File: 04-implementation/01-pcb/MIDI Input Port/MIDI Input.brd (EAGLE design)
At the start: 102.9 x 29.8 mm, 38 parts, among them J1 SDS-50J, J2 SDS-50J, J3 SDS-50J, J4 SDS-50J, J5 SSW-107-02-S-D, U1 PC900V, U2 PC900V, U3 PC900V, U4 PC900V

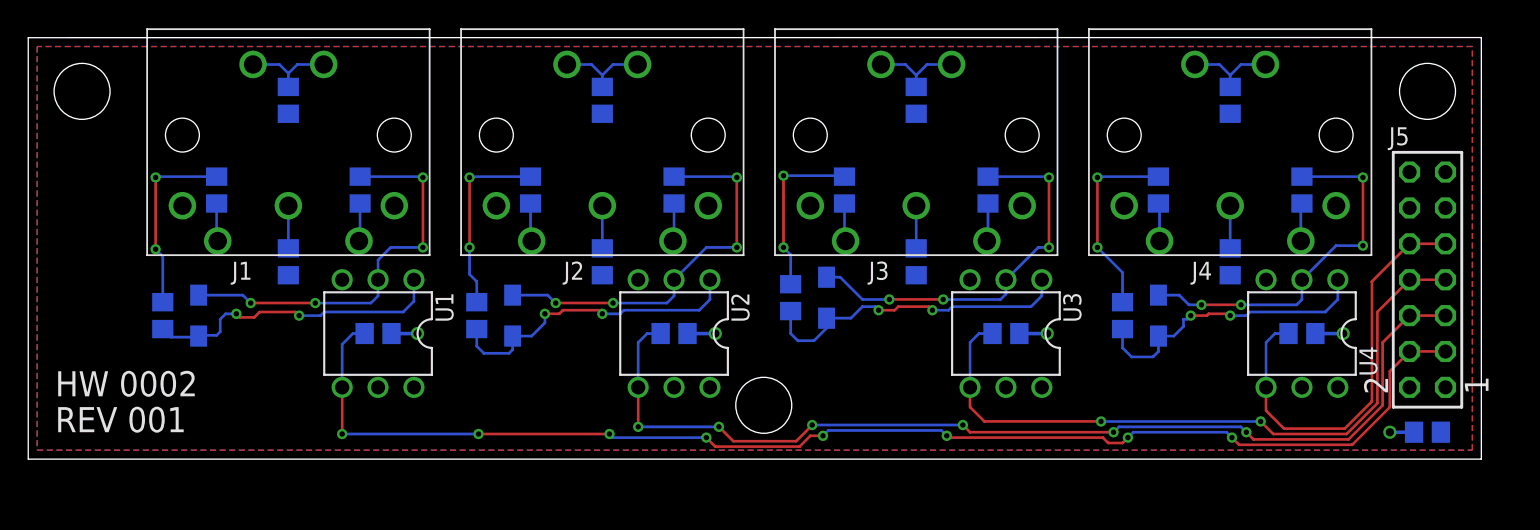
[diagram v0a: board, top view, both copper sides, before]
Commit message: Revise MIDI PCB's for mechanical spacing of ribbon connector.
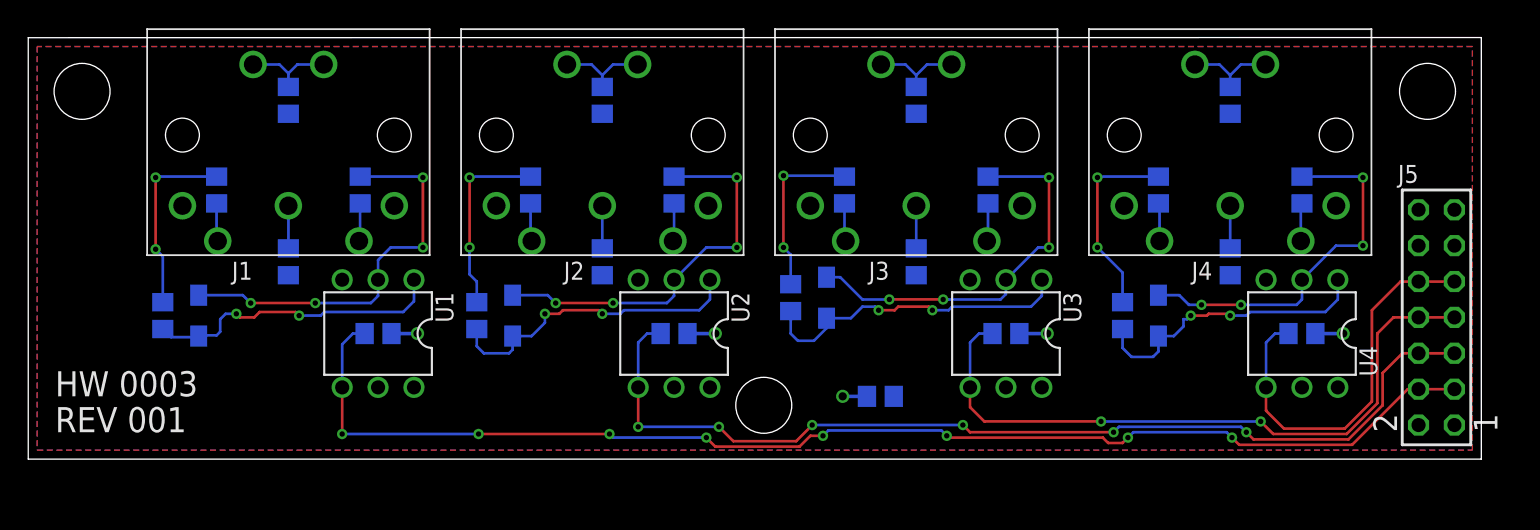
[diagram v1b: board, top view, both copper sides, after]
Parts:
- moved C9 38.8 mm to (60.3, 4.45)
- moved J5 2.74 mm to (99.7, 10.0)
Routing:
- net D-IN1: track 92.5 -> 90.5 mm
- net D-IN2: track 72.8 -> 71.1 mm
- net D-IN4: track 30.3 -> 28.6 mm
- net D-IN3: track 49.2 -> 47.8 mm
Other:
- board text added: "HW 0003"
- board text removed: "HW 0002"
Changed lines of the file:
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@@
 <?xml version="1.0" encoding="utf-8"?>
 <!DOCTYPE eagle SYSTEM "eagle.dtd">
-<eagle version="8.4.0">
+<eagle version="9.0.1">
 <drawing>
 <settings>
@@
 <setting verticaltext="up"/>
 </settings>
-<grid distance="25" unitdist="mil" unit="mil" style="lines" multiple="1" display="yes" altdistance="5" altunitdist="mil" altunit="mil"/>
+<grid distance="5" unitdist="mil" unit="mil" style="lines" multiple="1" display="yes" altdistance="5" altunitdist="mil" altunit="mil"/>
 <layers>
 <layer number="1" name="Top" color="4" fill="1" visible="yes" active="yes"/>
@@
 <hole x="52.07" y="3.81" drill="3.9624"/>
 <hole x="99.06" y="26.035" drill="3.9624"/>
-<text x="1.905" y="4.445" size="1.778" layer="25">HW 0002</text>
+<text x="1.905" y="4.445" size="1.778" layer="25">HW 0003</text>
 <text x="1.905" y="1.905" size="1.778" layer="25">REV 001</text>
 </plain>
@@
 <param name="dpMaxLengthDifference" value="10mm"/>
 <param name="dpGapFactor" value="2.5"/>
+<param name="checkAngle" value="0"/>
 <param name="checkFont" value="1"/>
 <param name="checkRestrict" value="1"/>
 <param name="checkStop" value="0"/>
+<param name="checkValues" value="0"/>
 <param name="useDiameter" value="13"/>
 <param name="maxErrors" value="50"/>
@@
 <attribute name="VALUE" x="20.955" y="15.24" size="1.27" layer="28" rot="MR270"/>
 </element>
-<element name="J5" library="con-samtec" library_urn="urn:adsk.eagle:library:184" package="SSW-107-02-S-D" value="SSW-107-02-S-D" x="99.06" y="12.7" smashed="yes" rot="R90">
-<attribute name="MF" value="" x="99.06" y="12.7" size="1.778" layer="27" rot="R90" display="off"/>
-<attribute name="MPN" value="SSW-107-02-S-D" x="99.06" y="12.7" size="1.778" layer="27" rot="R90" display="off"/>
-<attribute name="NAME" x="97.79" y="23.495" size="1.27" layer="25" rot="R180"/>
-<attribute name="OC_FARNELL" value="unknown" x="99.06" y="12.7" size="1.778" layer="27" rot="R90" display="off"/>
-<attribute name="OC_NEWARK" value="11P9431" x="99.06" y="12.7" size="1.778" layer="27" rot="R90" display="off"/>
-<attribute name="VALUE" x="101.6" y="23.495" size="1.27" layer="27" rot="R180"/>
+<element name="J5" library="con-samtec" library_urn="urn:adsk.eagle:library:184" package="SSW-107-02-S-D" value="SSW-107-02-S-D" x="99.695" y="10.033" smashed="yes" rot="R90">
+<attribute name="MF" value="" x="99.695" y="10.033" size="1.778" layer="27" rot="R90" display="off"/>
+<attribute name="MPN" value="SSW-107-02-S-D" x="99.695" y="10.033" size="1.778" layer="27" rot="R90" display="off"/>
+<attribute name="NAME" x="98.425" y="20.828" size="1.27" layer="25" rot="R180"/>
+<attribute name="OC_FARNELL" value="unknown" x="99.695" y="10.033" size="1.778" layer="27" rot="R90" display="off"/>
+<attribute name="OC_NEWARK" value="11P9431" x="99.695" y="10.033" size="1.778" layer="27" rot="R90" display="off"/>
+<attribute name="VALUE" x="102.235" y="20.828" size="1.27" layer="27" rot="R180"/>
 </element>
 <element name="R1" library="rcl" library_urn="urn:adsk.eagle:library:334" package="R0805" package3d_urn="urn:adsk.eagle:package:23553/2" value="220" x="13.335" y="19.05" smashed="yes" rot="MR90">
@@
 <attribute name="VALUE" x="77.47" y="18.415" size="1.27" layer="28" rot="MR90"/>
 </element>
-<element name="C9" library="rcl" library_urn="urn:adsk.eagle:library:334" package="C0805" package3d_urn="urn:adsk.eagle:package:23617/2" value="100n" x="99.06" y="1.905" smashed="yes" rot="MR180">
-<attribute name="NAME" x="97.155" y="1.27" size="1.27" layer="26" rot="MR0"/>
-<attribute name="VALUE" x="97.79" y="4.445" size="1.27" layer="28" rot="MR180"/>
+<element name="C9" library="rcl" library_urn="urn:adsk.eagle:library:334" package="C0805" package3d_urn="urn:adsk.eagle:package:23617/2" value="100n" x="60.325" y="4.445" smashed="yes" rot="MR180">
+<attribute name="NAME" x="58.42" y="3.81" size="1.27" layer="26" rot="MR0"/>
+<attribute name="VALUE" x="59.055" y="6.985" size="1.27" layer="28" rot="MR180"/>
 </element>
 </elements>
@@
 </polygon>
 <contactref element="C9" pad="1"/>
-<wire x1="98.11" y1="1.905" x2="96.393" y2="1.905" width="0.254" layer="16"/>
-<via x="96.393" y="1.905" extent="1-16" drill="0.5842"/>
+<wire x1="59.375" y1="4.445" x2="57.658" y2="4.445" width="0.254" layer="16"/>
+<via x="57.658" y="4.445" extent="1-16" drill="0.5842"/>
 <wire x1="46.67" y1="8.89" x2="48.641" y2="8.89" width="0.254" layer="16"/>
 <via x="48.641" y="8.89" extent="1-16" drill="0.5842"/>
@@
 <contactref element="U2" pad="P$4"/>
 <contactref element="R4" pad="1"/>
-<wire x1="100.33" y1="10.16" x2="97.79" y2="10.16" width="0.1905" layer="1"/>
+<wire x1="100.965" y1="7.493" x2="98.425" y2="7.493" width="0.1905" layer="1"/>
 <wire x1="43.18" y1="5.08" x2="43.18" y2="8.255" width="0.1905" layer="16"/>
 <wire x1="43.18" y1="8.255" x2="43.815" y2="8.89" width="0.1905" layer="16"/>
 <wire x1="43.815" y1="8.89" x2="44.77" y2="8.89" width="0.1905" layer="16"/>
-<wire x1="97.79" y1="10.16" x2="95.885" y2="8.255" width="0.1905" layer="1"/>
 <wire x1="95.885" y1="3.81" x2="93.472" y2="1.397" width="0.1905" layer="1"/>
-<wire x1="95.885" y1="8.255" x2="95.885" y2="3.81" width="0.1905" layer="1"/>
 <wire x1="86.741" y1="1.397" x2="86.233" y2="1.905" width="0.1905" layer="1"/>
 <via x="86.233" y="1.905" extent="1-16" drill="0.381"/>
@@
 <wire x1="76.835" y1="1.905" x2="66.675" y2="1.905" width="0.1905" layer="1"/>
 <wire x1="54.356" y1="1.27" x2="49.911" y2="1.27" width="0.1905" layer="1"/>
+<wire x1="98.425" y1="7.493" x2="97.282" y2="7.493" width="0.1905" layer="1"/>
+<wire x1="97.282" y1="7.493" x2="95.885" y2="6.096" width="0.1905" layer="1"/>
+<wire x1="95.885" y1="6.096" x2="95.885" y2="3.81" width="0.1905" layer="1"/>
 </signal>
 <signal name="D-IN3">
@@
 <contactref element="U3" pad="P$4"/>
 <contactref element="R6" pad="1"/>
-<wire x1="100.33" y1="12.7" x2="97.79" y2="12.7" width="0.1905" layer="1"/>
+<wire x1="100.965" y1="10.033" x2="98.425" y2="10.033" width="0.1905" layer="1"/>
 <wire x1="66.675" y1="5.08" x2="66.675" y2="8.255" width="0.1905" layer="16"/>
 <wire x1="66.675" y1="8.255" x2="67.31" y2="8.89" width="0.1905" layer="16"/>
 <wire x1="67.31" y1="8.89" x2="68.265" y2="8.89" width="0.1905" layer="16"/>
-<wire x1="97.79" y1="12.7" x2="95.504" y2="10.414" width="0.1905" layer="1"/>
 <wire x1="95.504" y1="3.94985625" x2="93.33214375" y2="1.778" width="0.1905" layer="1"/>
-<wire x1="95.504" y1="10.414" x2="95.504" y2="3.94985625" width="0.1905" layer="1"/>
 <wire x1="88.138" y1="1.778" x2="87.249" y2="2.667" width="0.1905" layer="1"/>
 <via x="87.249" y="2.667" extent="1-16" drill="0.381"/>
@@
 <wire x1="66.675" y1="3.683" x2="66.675" y2="5.08" width="0.1905" layer="1"/>
 <wire x1="93.33214375" y1="1.778" x2="88.138" y2="1.778" width="0.1905" layer="1"/>
+<wire x1="98.425" y1="10.033" x2="96.647" y2="10.033" width="0.1905" layer="1"/>
+<wire x1="96.647" y1="10.033" x2="95.504" y2="8.89" width="0.1905" layer="1"/>
+<wire x1="95.504" y1="8.89" x2="95.504" y2="3.94985625" width="0.1905" layer="1"/>
 </signal>
 <signal name="D-IN4">
@@
 <contactref element="U4" pad="P$4"/>
 <contactref element="R8" pad="1"/>
-<wire x1="100.33" y1="15.24" x2="97.79" y2="15.24" width="0.1905" layer="1"/>
+<wire x1="100.965" y1="12.573" x2="98.425" y2="12.573" width="0.1905" layer="1"/>
 <wire x1="87.63" y1="5.08" x2="87.63" y2="8.255" width="0.1905" layer="16"/>
 <wire x1="87.63" y1="8.255" x2="88.265" y2="8.89" width="0.1905" layer="16"/>
 <wire x1="88.265" y1="8.89" x2="89.22" y2="8.89" width="0.1905" layer="16"/>
-<wire x1="97.79" y1="15.24" x2="95.123" y2="12.573" width="0.1905" layer="1"/>
-<wire x1="95.123" y1="4.0897125" x2="93.1922875" y2="2.159" width="0.1905" layer="1"/>
+<wire x1="93.1922875" y1="2.159" x2="95.123" y2="4.0897125" width="0.1905" layer="1"/>
 <wire x1="88.9" y1="2.159" x2="87.63" y2="3.429" width="0.1905" layer="1"/>
 <wire x1="87.63" y1="3.429" x2="87.63" y2="5.08" width="0.1905" layer="1"/>
-<wire x1="95.123" y1="12.573" x2="95.123" y2="4.0897125" width="0.1905" layer="1"/>
 <wire x1="93.1922875" y1="2.159" x2="88.9" y2="2.159" width="0.1905" layer="1"/>
+<wire x1="98.425" y1="12.573" x2="97.155" y2="12.573" width="0.1905" layer="1"/>
+<wire x1="97.155" y1="12.573" x2="95.123" y2="10.541" width="0.1905" layer="1"/>
+<wire x1="95.123" y1="4.0897125" x2="95.123" y2="10.541" width="0.1905" layer="1"/>
 </signal>
 <signal name="D-IN1">
@@
 <wire x1="22.225" y1="8.128" x2="22.987" y2="8.89" width="0.1905" layer="16"/>
 <wire x1="22.987" y1="8.89" x2="23.815" y2="8.89" width="0.1905" layer="16"/>
-<wire x1="100.33" y1="7.62" x2="97.79" y2="7.62" width="0.1905" layer="1"/>
-<wire x1="97.79" y1="7.62" x2="96.393" y2="6.223" width="0.1905" layer="1"/>
-<wire x1="96.393" y1="6.223" x2="96.393" y2="3.683" width="0.1905" layer="1"/>
-<wire x1="96.393" y1="3.683" x2="93.726" y2="1.016" width="0.1905" layer="1"/>
+<wire x1="100.965" y1="4.953" x2="98.425" y2="4.953" width="0.1905" layer="1"/>
 <wire x1="85.725" y1="1.016" x2="85.217" y2="1.524" width="0.1905" layer="1"/>
 <via x="85.217" y="1.524" extent="1-16" drill="0.381"/>
@@
 <wire x1="77.47" y1="1.143" x2="76.454" y2="1.143" width="0.1905" layer="1"/>
 <wire x1="76.454" y1="1.143" x2="76.073" y2="1.524" width="0.1905" layer="1"/>
-<wire x1="93.726" y1="1.016" x2="85.725" y2="1.016" width="0.1905" layer="1"/>
+<wire x1="85.725" y1="1.016" x2="93.726" y2="1.016" width="0.1905" layer="1"/>
 <wire x1="84.836" y1="1.905" x2="78.232" y2="1.905" width="0.1905" layer="16"/>
 <wire x1="65.151" y1="1.524" x2="65.024" y2="1.651" width="0.1905" layer="1"/>
@@
 <wire x1="76.073" y1="1.524" x2="65.151" y2="1.524" width="0.1905" layer="1"/>
 <wire x1="64.643" y1="2.032" x2="56.642" y2="2.032" width="0.1905" layer="16"/>
+<wire x1="97.663" y1="4.953" x2="98.425" y2="4.953" width="0.1905" layer="1"/>
+<wire x1="93.726" y1="1.016" x2="97.663" y2="4.953" width="0.1905" layer="1"/>
 </signal>
 <signal name="N$1">

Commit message: Add files for PCB releases.
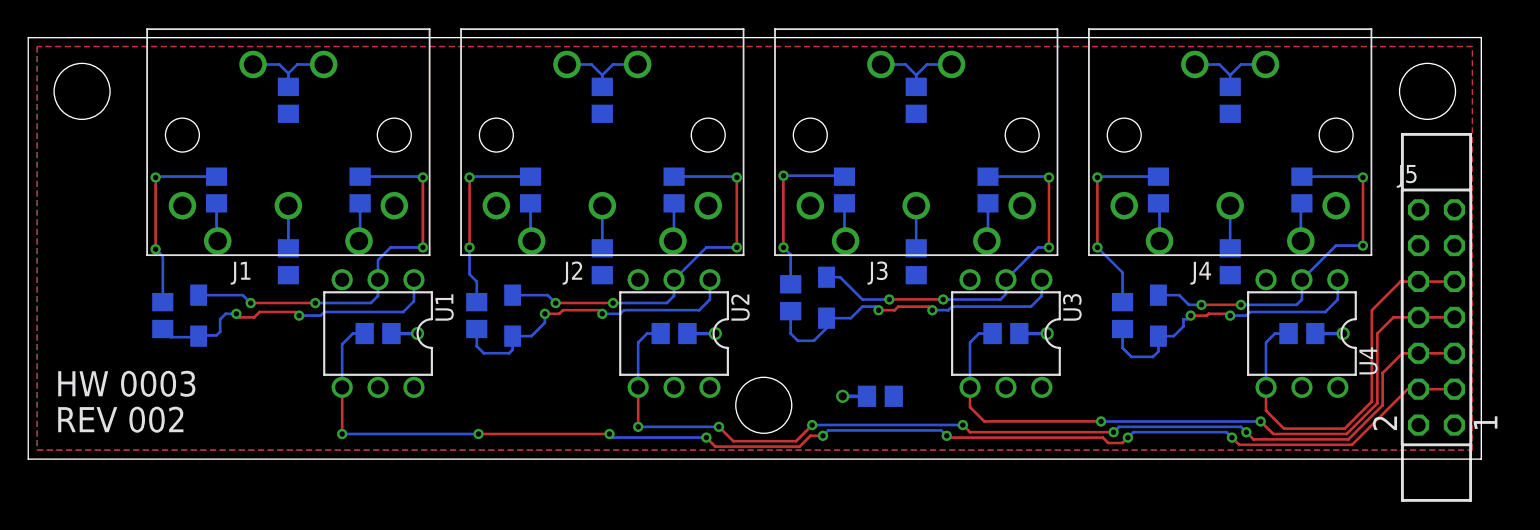
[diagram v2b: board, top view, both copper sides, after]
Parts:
- J5: value SSW-107-02-S-D -> SSW-107-02-G-D; device con-samtec:SSW-107-02-S-D -> MIDI router parts:SSW-107-02-G-D
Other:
- board text added: "REV 002"
- board text removed: "REV 001"
